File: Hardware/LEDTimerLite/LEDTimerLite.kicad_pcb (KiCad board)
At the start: 4 copper layers, 49.5 x 16.3 mm, 28 parts, among them J1 Program, J2 LED, J3 PWR, Q1 S8050, SW1 SW_Push, SW4 SW_PWR, U1 AP7383-36WW7, U2 PIC16LF18326, U4 BCR_421U_E6327, Y1 32.768 kHz

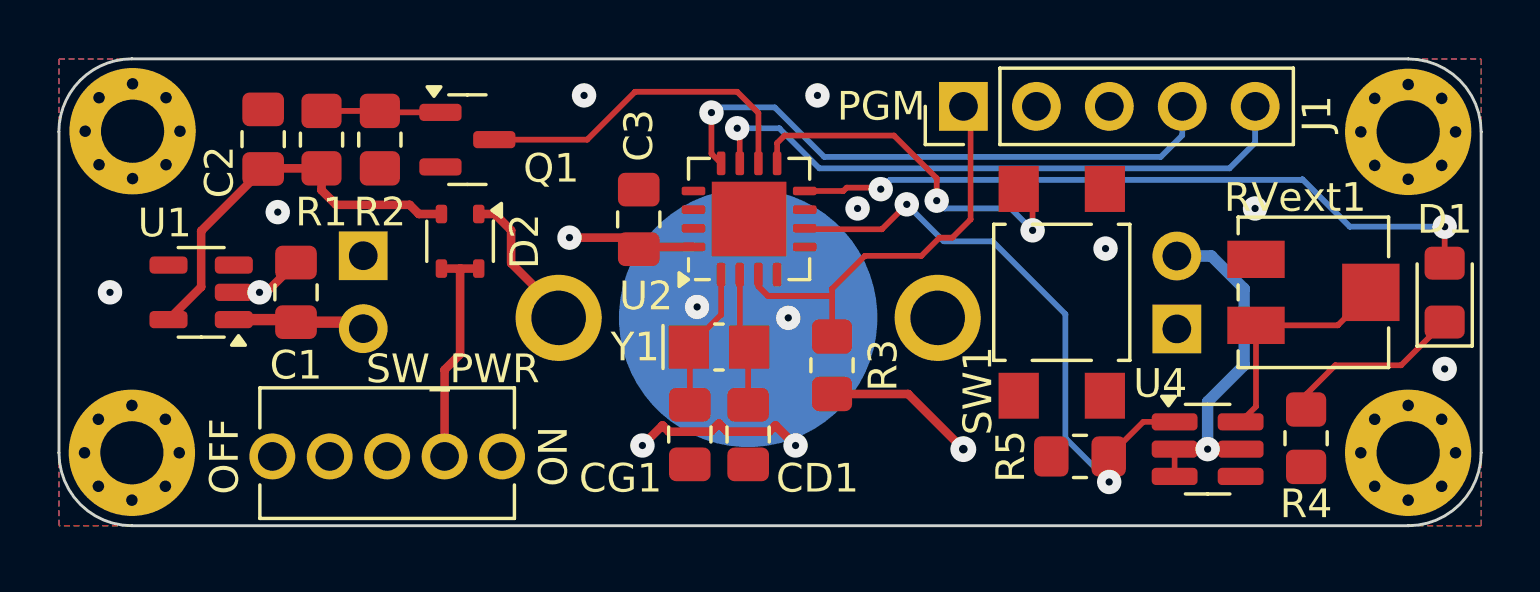
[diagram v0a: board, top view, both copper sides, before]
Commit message: LTL: add extra test points, optimize layout
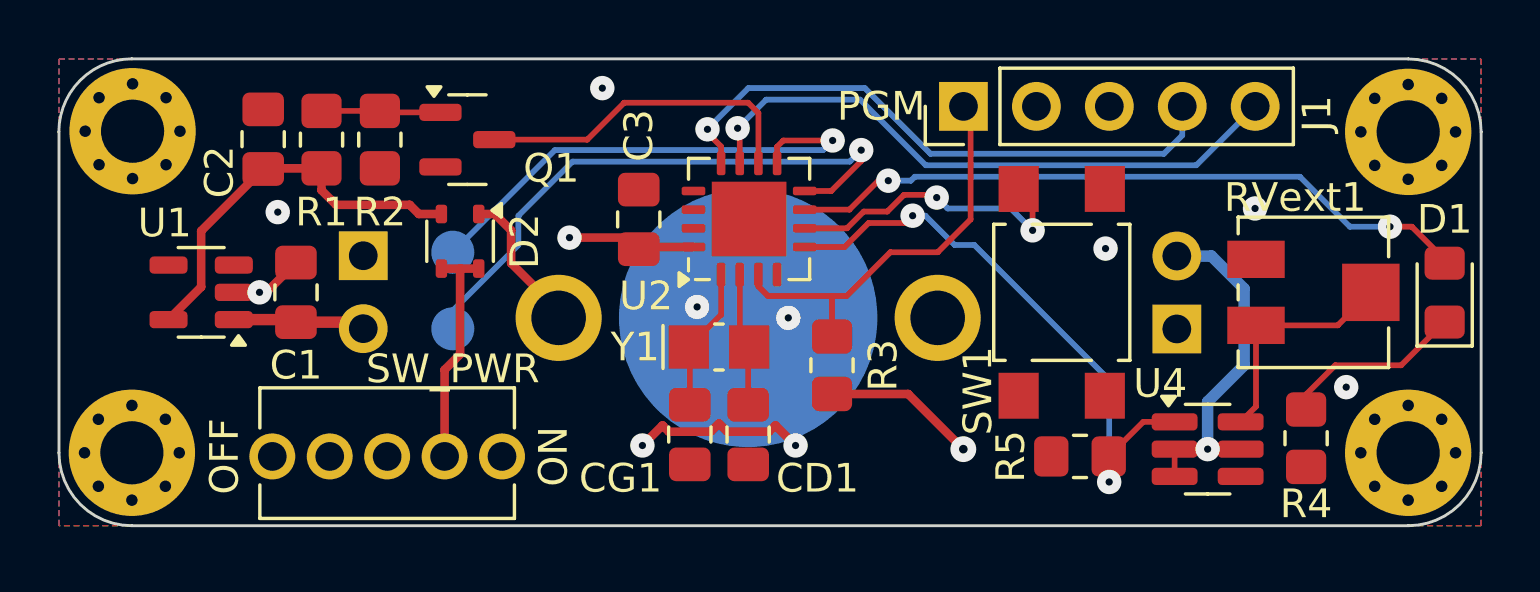
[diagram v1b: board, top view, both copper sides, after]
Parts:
- added TP1: TestPoint, TestPoint:TestPoint_Pad_D1.5mm, B.Cu at (104.3, 63.4)
- added TP2: TestPoint, TestPoint:TestPoint_Pad_D1.5mm, B.Cu at (104.3, 66.0)
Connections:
- SW1 pad 2: Net-(U2-RC0) -> /SW
- U2 pad 5: unconnected-(U2-RC4-Pad5) -> /LED_EN_PWM
- U2 pad 6: /LED_EN_PWM -> /SW
- U2 pad 7: unconnected-(U2-RC2-Pad7) -> /LED
- U2 pad 8: /LED -> /TP2
- U2 pad 9: Net-(U2-RC0) -> /TP1
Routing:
- net /TP2: track 0.00 -> 20.5 mm, vias 0 -> 1
- net /TP1: track 0.00 -> 17.4 mm, vias 0 -> 1
- net Net-(U2-RC0): track 13.2 -> 0.00 mm, vias 2 -> 0
- net /SW: track 0.00 -> 10.6 mm, vias 0 -> 2
- net GND: vias 13 -> 10

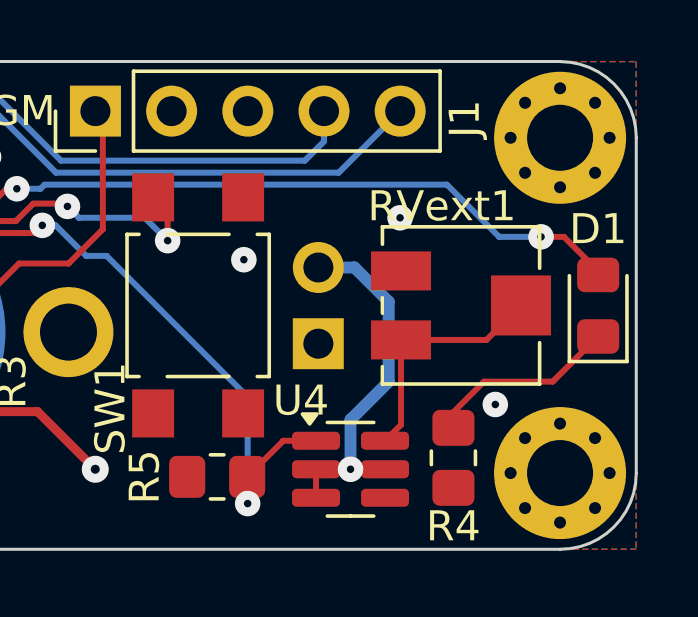
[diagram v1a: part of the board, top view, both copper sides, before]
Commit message: LTL: replace LED driver and RVext1
Use BCR321U (250 mA) instead of BCR421U (150 mA).
Use TC33X-2-101E as RVext1 because it's cheaper.
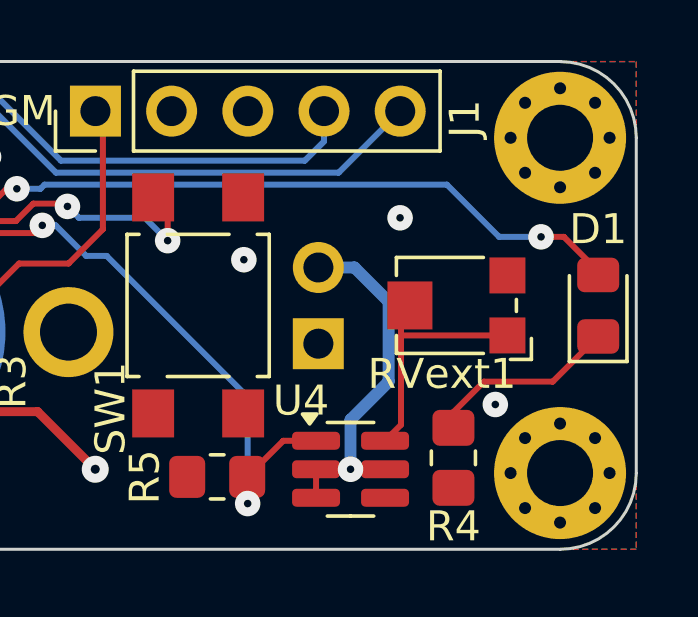
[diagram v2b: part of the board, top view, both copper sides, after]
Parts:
- RVext1: footprint Potentiometer_SMD:Potentiometer_Vishay_TS53YJ_Vertical -> Potentiometer_SMD:Potentiometer_Bourns_TC33X_Vertical
- U4: value BCR_421U_E6327 -> BCR_321U_E6327
- moved RVext1 0.25 mm to (134.0, 64.8)
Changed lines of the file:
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@@
 		)
 	)
-	(footprint "Potentiometer_SMD:Potentiometer_Vishay_TS53YJ_Vertical"
+	(footprint "Potentiometer_SMD:Potentiometer_Bourns_TC33X_Vertical"
 		(layer "F.Cu")
-		(at 134.239 64.77 180)
-		(descr "Potentiometer, vertical, Vishay TS53YJ, https://www.vishay.com/docs/51008/ts53.pdf")
-		(tags "Potentiometer vertical Vishay TS53YJ")
+		(at 133.985 64.77 180)
+		(descr "Potentiometer, Bourns, TC33X, Vertical, https://www.bourns.com/pdfs/TC33.pdf")
+		(tags "Potentiometer Bourns TC33X Vertical")
 		(property "Reference" "RVext1"
-			(at 0.635 3.302 0)
+			(at 0.381 -2.286 180)
 			(layer "F.SilkS")
 			(effects
@@
 		)
 		(property "Value" "R_Potentiometer"
-			(at 0 3.75 0)
+			(at 0 2.5 180)
 			(layer "F.Fab")
 			(effects
@@
 			)
 		)
-		(property "Footprint" "Potentiometer_SMD:Potentiometer_Vishay_TS53YJ_Vertical"
+		(property "Footprint" "Potentiometer_SMD:Potentiometer_Bourns_TC33X_Vertical"
 			(at 0 0 180)
 			(unlocked yes)
@@
 		(attr smd)
 		(fp_line
-			(start 2.62 2.04)
-			(end 2.62 2.62)
+			(start 1.9 1.6)
+			(end 1.9 1)
 			(stroke
 				(width 0.12)
@@
 		)
 		(fp_line
-			(start 2.62 -0.26)
-			(end 2.62 0.26)
+			(start 1.9 -1.6)
+			(end 1.9 -1)
 			(stroke
 				(width 0.12)
@@
 		)
 		(fp_line
-			(start 2.62 -2.62)
-			(end 2.62 -2.039)
+			(start -1 1.6)
+			(end 1.9 1.6)
 			(stroke
 				(width 0.12)
@@
 		)
 		(fp_line
-			(start -2.62 2.62)
-			(end 2.62 2.62)
+			(start -1 -1.6)
+			(end 1.9 -1.6)
 			(stroke
 				(width 0.12)
@@
 		)
 		(fp_line
-			(start -2.62 1.24)
-			(end -2.62 2.62)
+			(start -1.9 -1.8)
+			(end -2.6 -1.8)
 			(stroke
 				(width 0.12)
@@
 		)
 		(fp_line
-			(start -2.62 -2.62)
-			(end 2.62 -2.62)
+			(start -2.1 -0.2)
+			(end -2.1 0.2)
 			(stroke
 				(width 0.12)
@@
 		)
 		(fp_line
-			(start -2.62 -2.62)
-			(end -2.62 -1.24)
+			(start -2.6 -1.8)
+			(end -2.6 -1.1)
 			(stroke
 				(width 0.12)
@@
 			(layer "F.SilkS")
 		)
-		(fp_line
-			(start 3.25 2.75)
-			(end 3.25 -2.75)
+		(fp_circle
+			(center 0 0)
+			(end 1.8 0)
 			(stroke
 				(width 0.05)
 				(type solid)
 			)
-			(layer "F.CrtYd")
+			(fill none)
+			(layer "Dwgs.User")
 		)
 		(fp_line
-			(start 3.25 -2.75)
-			(end -3.25 -2.75)
+			(start 2.45 1.85)
+			(end -2.65 1.85)
 			(stroke
 				(width 0.05)
@@
 		)
 		(fp_line
-			(start -3.25 2.75)
-			(end 3.25 2.75)
+			(start 2.45 -1.85)
+			(end 2.45 1.85)
 			(stroke
 				(width 0.05)
@@
 		)
 		(fp_line
-			(start -3.25 -2.75)
-			(end -3.25 2.75)
+			(start -2.65 1.85)
+			(end -2.65 -1.85)
 			(stroke
 				(width 0.05)
@@
 		)
 		(fp_line
-			(start 2.5 2.5)
-			(end 2.5 -2.5)
-			(stroke
-				(width 0.1)
-				(type solid)
-			)
-			(layer "F.Fab")
-		)
-		(fp_line
-			(start 2.5 -2.5)
-			(end -2.5 -2.5)
-			(stroke
-				(width 0.1)
-				(type solid)
-			)
-			(layer "F.Fab")
-		)
-		(fp_line
-			(start 0.92 0.058)
-			(end 0.058 0.058)
-			(stroke
-				(width 0.1)
-				(type solid)
-			)
-			(layer "F.Fab")
-		)
-		(fp_line
-			(start 0.92 -0.058)
-			(end 0.92 0.058)
-			(stroke
-				(width 0.1)
-				(type solid)
-			)
-			(layer "F.Fab")
-		)
-		(fp_line
-			(start 0.058 0.92)
-			(end -0.058 0.92)
-			(stroke
-				(width 0.1)
-				(type solid)
-			)
-			(layer "F.Fab")
-		)
-		(fp_line
-			(start 0.058 0.058)
-			(end 0.058 0.92)
-			(stroke
-				(width 0.1)
-				(type solid)
-			)
-			(layer "F.Fab")
-		)
-		(fp_line
-			(start 0.058 -0.058)
-			(end 0.92 -0.058)
-			(stroke
-				(width 0.1)
-				(type solid)
-			)
-			(layer "F.Fab")
-		)
-		(fp_line
-			(start 0.058 -0.92)
-			(end 0.058 -0.058)
-			(stroke
-				(width 0.1)
-				(type solid)
-			)
-			(layer "F.Fab")
-		)
-		(fp_line
-			(start -0.058 0.92)
-			(end -0.058 0.058)
-			(stroke
-				(width 0.1)
-				(type solid)
-			)
-			(layer "F.Fab")
-		)
-		(fp_line
-			(start -0.058 0.058)
-			(end -0.92 0.058)
+			(start -2.65 -1.85)
+			(end 2.45 -1.85)
 			(stroke
-				(width 0.1)
-				(type solid)
-			)
-			(layer "F.Fab")
-		)
-		(fp_line
-			(start -0.058 -0.058)
-			(end -0.058 -0.92)
-			(stroke
-				(width 0.1)
+				(width 0.05)
 				(type solid)
 			)
-			(layer "F.Fab")
+			(layer "F.CrtYd")
 		)
 		(fp_line
-			(start -0.058 -0.92)
-			(end 0.058 -0.92)
+			(start 1.8 1.5)
+			(end 1.8 -1.5)
 			(stroke
 				(width 0.1)
@@
 		)
 		(fp_line
-			(start -0.92 0.058)
-			(end -0.92 -0.058)
+			(start 1.8 -1.5)
+			(end -1.25 -1.5)
 			(stroke
 				(width 0.1)
@@
 		)
 		(fp_line
-			(start -0.92 -0.058)
-			(end -0.058 -0.058)
+			(start -1.25 -1.5)
+			(end -2 -0.75)
 			(stroke
 				(width 0.1)
@@
 		)
 		(fp_line
-			(start -2.5 2.5)
-			(end 2.5 2.5)
+			(start -2 1.5)
+			(end 1.8 1.5)
 			(stroke
 				(width 0.1)
@@
 		)
 		(fp_line
-			(start -2.5 -2.5)
-			(end -2.5 2.5)
+			(start -2 -0.75)
+			(end -2 1.5)
 			(stroke
 				(width 0.1)
@@
 		(fp_circle
 			(center 0 0)
-			(end 1.15 0)
+			(end 1.5 0)
 			(stroke
 				(width 0.1)
@@
 			(layer "F.Fab")
 		)
+		(fp_text user "Wiper may be\nanywhere within\ncircle shown"
+			(at -0.15 -0.8 180)
+			(layer "Cmts.User")
+			(effects
+				(font
+					(size 0.15 0.15)
+					(thickness 0.02)
+				)
+			)
+		)
 		(fp_text user "${REFERENCE}"
-			(at 0 -2 0)
+			(at 0 0 180)
 			(layer "F.Fab")
 			(effects
 				(font
-					(size 0.68 0.68)
-					(thickness 0.15)
+					(size 0.7 0.7)
+					(thickness 0.105)
 				)
 			)
 		)
 		(pad "1" smd rect
-			(at 2 -1.15 180)
-			(size 2 1.3)
+			(at -1.8 -1 180)
+			(size 1.2 1.2)
 			(layers "F.Cu" "F.Paste" "F.Mask")
 			(net 11 "Net-(U4-Rext)")
@@
 		)
 		(pad "2" smd rect
-			(at -2 0 180)
-			(size 2 2)
+			(at 1.45 0 180)
+			(size 1.5 1.6)
 			(layers "F.Cu" "F.Paste" "F.Mask")
 			(net 11 "Net-(U4-Rext)")
@@
 		)
 		(pad "3" smd rect
-			(at 2 1.15 180)
-			(size 2 1.3)
+			(at -1.8 1 180)
+			(size 1.2 1.2)
 			(layers "F.Cu" "F.Paste" "F.Mask")
 			(net 2 "GND")
@@
 			(pintype "passive")
 		)
-		(model "${KICAD8_3DMODEL_DIR}/Potentiometer_SMD.3dshapes/Potentiometer_Bourns_3314G_Vertical.wrl"
+		(model "${KIPRJMOD}/LIB_TC33X-2-101E/TC33X-2-101E.stp"
 			(offset
 				(xyz 0 0 0)
@@
 			)
 			(rotate
-				(xyz 0 0 90)
+				(xyz -90 0 90)
 			)
 		)
@@
 			)
 		)
-		(property "Value" "BCR_421U_E6327"
+		(property "Value" "BCR_321U_E6327"
 			(at 0 2.4 360)
 			(layer "F.Fab")
@@
 			)
 		)
-		(property "Datasheet" "https://4donline.ihs.com/images/VipMasterIC/IC/INFN/INFN-S-A0000798853/INFN-S-A0000798853-1.pdf?hkey=6D3A4C79FDBF58556ACFDE234799DDF0"
+		(property "Datasheet" "https://www.infineon.com/dgdl/Infineon-BCR320U_BCR321U-DataSheet-v02_02-EN.pdf?fileId=5546d4624b0b249c014b7d69949b463b"
 			(at 0 0 360)
 			(layer "F.Fab")
@@
 	)
 	(segment
+		(start 131.706 69.281)
+		(end 132.239 68.748)
+		(width 0.2)
+		(layer "F.Cu")
+		(net 11)
+	)
+	(segment
+		(start 132.255 65.77)
+		(end 132.239 65.786)
+		(width 0.2)
+		(layer "F.Cu")
+		(net 11)
+	)
+	(segment
 		(start 132.239 68.748)
-		(end 132.239 65.92)
+		(end 132.239 65.786)
 		(width 0.2)
 		(layer "F.Cu")
@@
 	)
 	(segment
-		(start 131.706 69.281)
-		(end 132.239 68.748)
+		(start 132.239 65.066)
+		(end 132.535 64.77)
 		(width 0.2)
 		(layer "F.Cu")
@@
 	)
 	(segment
-		(start 135.089 65.92)
-		(end 132.239 65.92)
+		(start 132.239 65.786)
+		(end 132.239 65.066)
 		(width 0.2)
 		(layer "F.Cu")
@@
 	)
 	(segment
-		(start 136.239 64.77)
-		(end 135.089 65.92)
+		(start 135.785 65.77)
+		(end 132.255 65.77)
 		(width 0.2)
 		(layer "F.Cu")

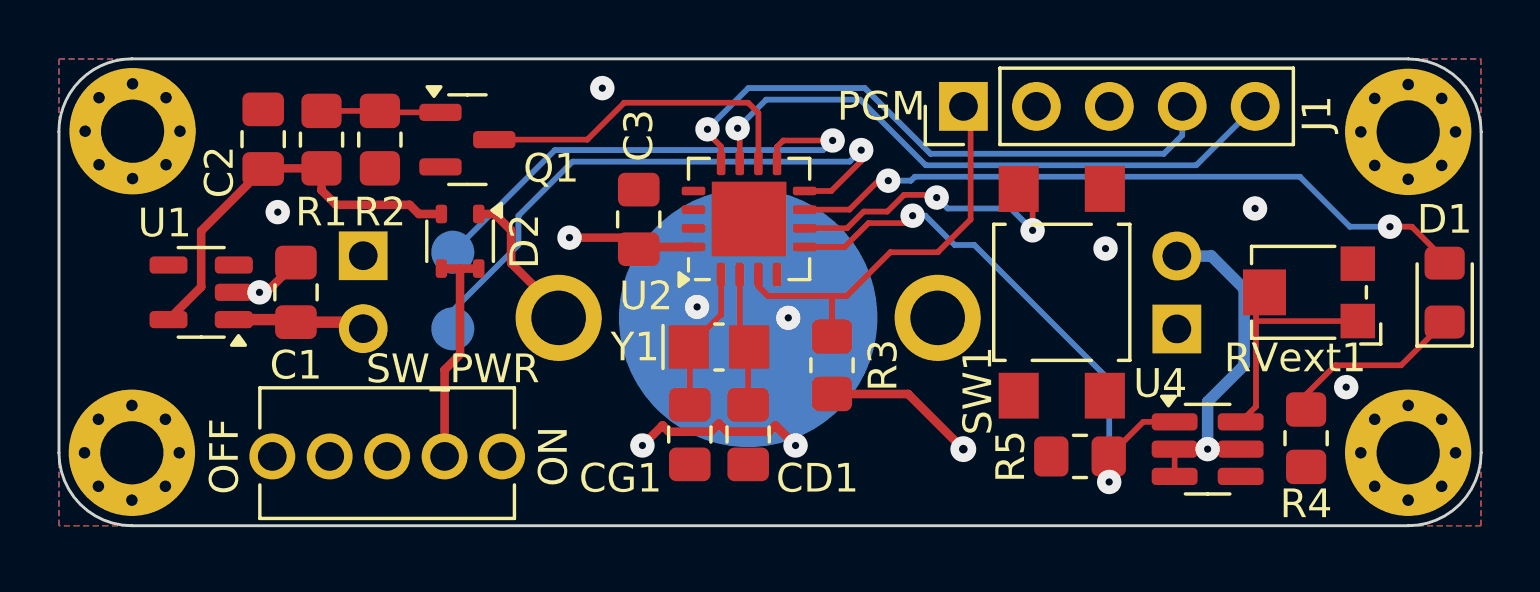
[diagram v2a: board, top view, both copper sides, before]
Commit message: LTL: add debouncing capacitor to SW
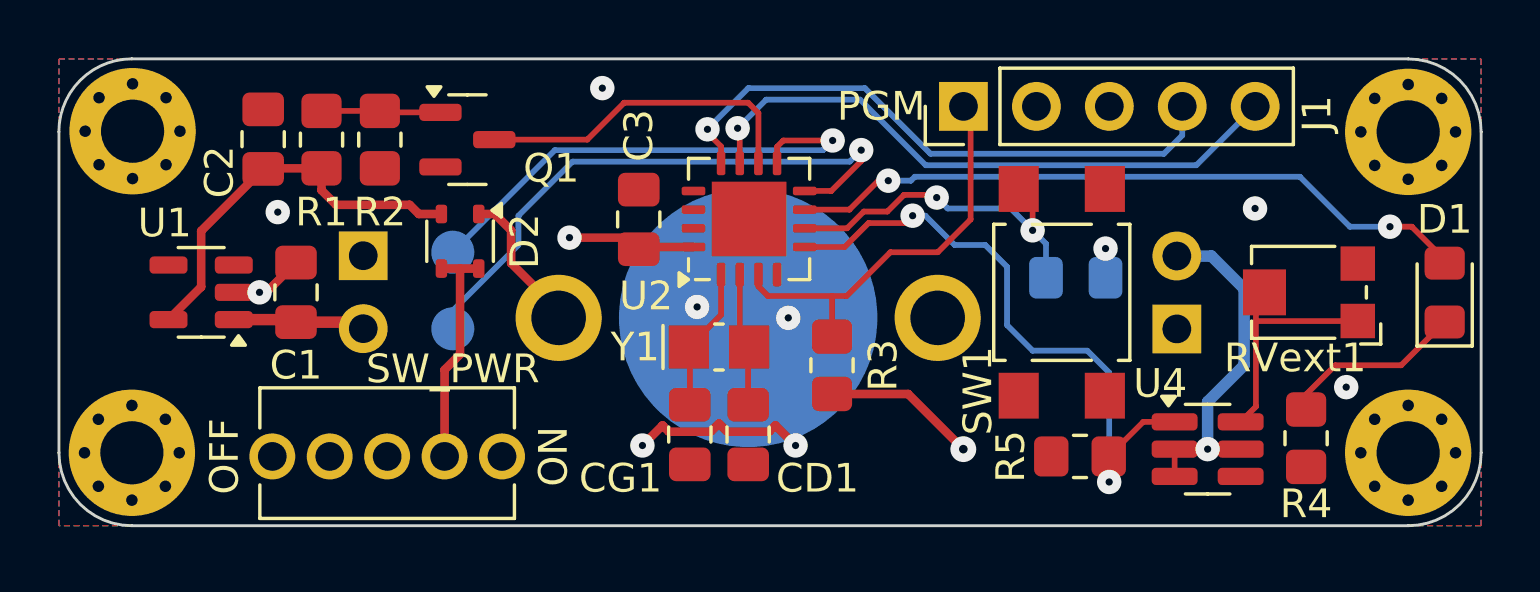
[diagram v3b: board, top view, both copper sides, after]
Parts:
- added C4: 100n, Capacitor_SMD:C_0805_2012Metric_Pad1.18x1.45mm_HandSolder, B.Cu at (126.0, 64.3)
- U1: value AP7383-36WW7 -> AP7383-33WW7
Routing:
- net /SW: track 10.6 -> 12.5 mm
- net /LED_EN_PWM: track 20.9 -> 22.2 mm
- net GND: track 8.03 -> 9.05 mm
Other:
- board text added: "CR1216/20"
- board text removed: "CR1220"
